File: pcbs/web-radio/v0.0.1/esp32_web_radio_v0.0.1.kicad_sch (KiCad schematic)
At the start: 56 parts, among them IC1 TLV320DAC3100IRHBR, J1 AudioJack4, J3 USB4085-GF-A_REVB, J4 Conn_01x02_Pin, SW1 BOOT, SW2 RESET, SW3 VOLUME_UP, SW6 SW_Slide_DPDT, SW7 VOLUME_DOWN, SW8 MUTE, U1 TLV320AIC3100, U2 ESP32-S3-WROOM-1, U3 AP2127K-1.8, U4 LD39200PUR

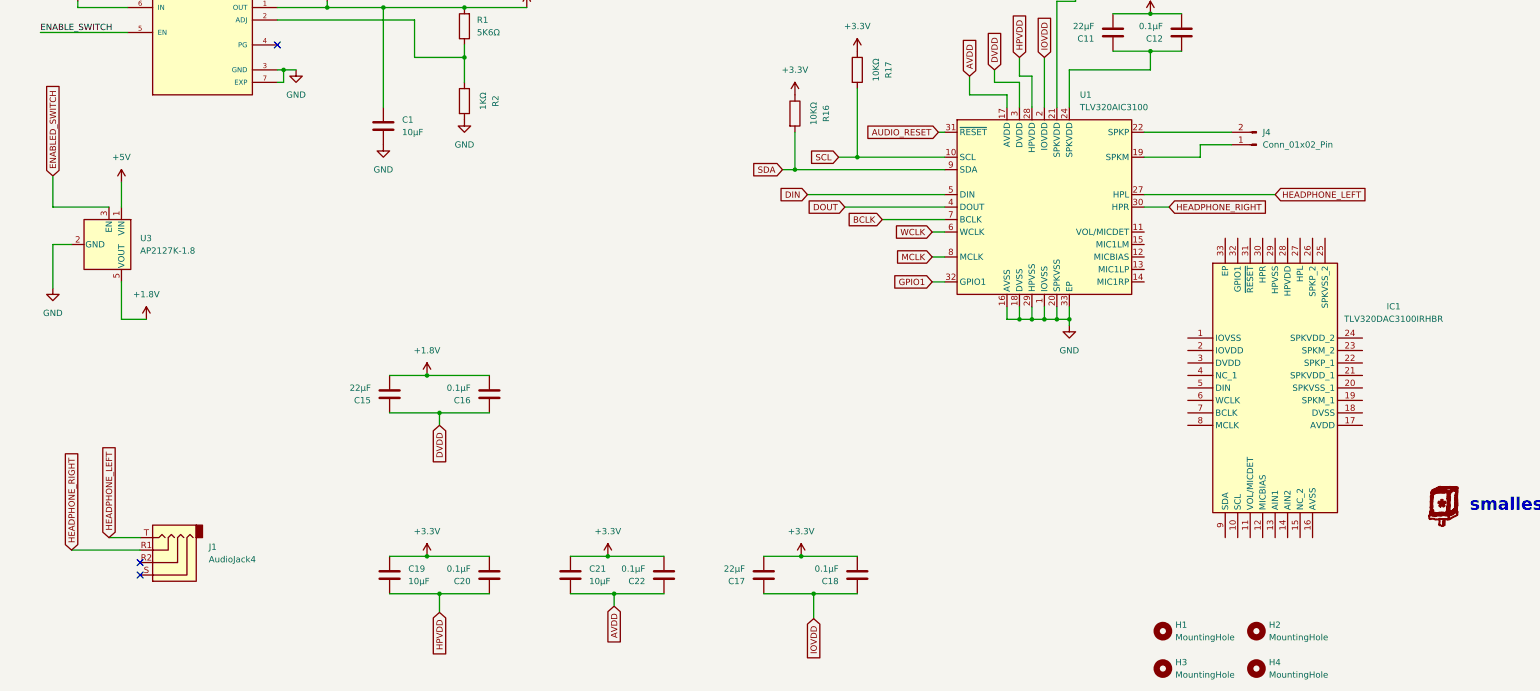
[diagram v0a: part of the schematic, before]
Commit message: adding libraries
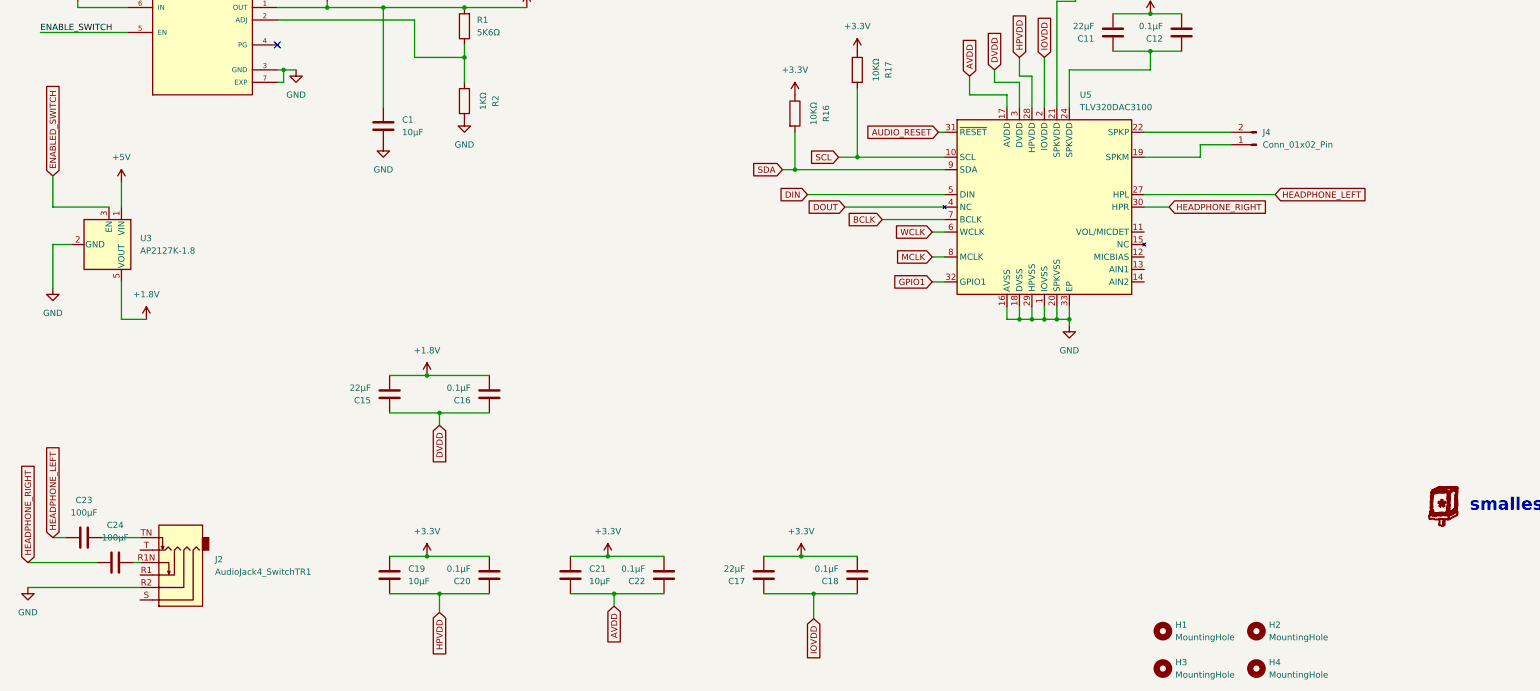
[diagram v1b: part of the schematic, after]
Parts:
- removed IC1: TLV320DAC3100IRHBR, QFN50P500X500X100-33N-D, symbol TLV320DAC:TLV320DAC3100IRHBR
- removed J1: AudioJack4, symbol Connector_Audio:AudioJack4
- removed U1: TLV320AIC3100, Package_DFN_QFN:VQFN-32-1EP_5x5mm_P0.5mm_EP3.5x3.5mm, symbol Audio:TLV320AIC3100
- added C23: 100µF, Capacitor_SMD:C_1206_3216Metric_Pad1.33x1.80mm_HandSolder, symbol Device:C
- added C24: 100µF, Capacitor_SMD:C_0805_2012Metric_Pad1.18x1.45mm_HandSolder, symbol Device:C
- added J2: AudioJack4_SwitchTR1, symbol Connector_Audio:AudioJack4_SwitchTR1
- added U5: TLV320DAC3100, Package_DFN_QFN:VQFN-32-1EP_5x5mm_P0.5mm_EP3.5x3.5mm, symbol smallest-space-hardware/libs:TLV320DAC3100
- J3: footprint USB4085-GF-A_REVB:GCT_USB4085-GF-A_REVB -> smallest-space-hardware/libs:GCT_USB4085-GF-A_REVB
- U4: footprint LD39200PUR:SON95P300X300X100-7N -> smallest-space-hardware/libs:SON95P300X300X100-7N
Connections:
- net AUDIO_RESET: now also U5.31 (~{RESET})
- net AVDD: now also U5.17 (AVDD)
- net BCLK: now also U5.7 (BCLK)
- net DIN: now also U5.5 (DIN)
- net DOUT: now also U5.4 (NC)
- net DVDD: now also U5.3 (DVDD)
- net GND: now also J2.R2, U5.1 (IOVSS), U5.16 (AVSS), U5.18 (DVSS), U5.20 (SPKVSS), U5.25 (SPKVSS), U5.29 (HPVSS), U5.33 (EP)
- net GPIO1: now also U5.32 (GPIO1)
- net HEADPHONE_LEFT: now also C23.2, U5.27 (HPL)
- net HEADPHONE_RIGHT: now also C24.2, U5.30 (HPR)
- net HPVDD: now also U5.28 (HPVDD)
- net IOVDD: now also U5.2 (IOVDD)
- net MCLK: now also U5.8 (MCLK)
- net SCL: now also U5.10 (SCL)
- net SDA: now also U5.9 (SDA)
- net WCLK: now also U5.6 (WCLK)
- net at C13.1, C14.1: now also U5.21 (SPKVDD)
- net at J4.1 (Pin_1): now also U5.19 (SPKM), U5.23 (SPKM)
- net at J4.2 (Pin_2): now also U5.22 (SPKP), U5.26 (SPKP)
- net at C11.1, C12.1: now also U5.24 (SPKVDD)
- new net: C24.1, J2.R1N
- new net: C23.1, J2.TN
- no-connect marks 25 -> 23

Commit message: fix libraries and update schematics
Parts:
- J1: renamed from J3; footprint smallest-space-hardware/libs:GCT_USB4085-GF-A_REVB -> smallest.space:GCT_USB4085-GF-A_REVB
- U2: renamed from U4; footprint smallest-space-hardware/libs:SON95P300X300X100-7N -> smallest.space:SON95P300X300X100-7N
- renumbered C23 to C1, C17 to C10, C6 to C11, C7 to C12, C8 to C13, C18 to C14, C14 to C15, C13 to C16, C11 to C17, C4 to C18, C12 to C19, C24 to C2, C5 to C20, C2 to C21, C3 to C22, C1 to C3, C15 to C4, C19 to C5, C16 to C6, C20 to C7, C21 to C8, C22 to C9, D5 to D1, D4 to D2, D1 to D3, H3 to H2, H2 to H3, J4 to J3, R7 to R1, R6 to R10, R14 to R11, R15 to R12, R3 to R13, R12 to R14, R4 to R15, R8 to R2, R5 to R3, R9 to R4, R1 to R5, R2 to R6, R16 to R7, R13 to R8, R17 to R9, SW6 to SW1, SW3 to SW2, SW7 to SW3, SW8 to SW4, SW2 to SW5, SW1 to SW6, U3 to U1, U5 to U3, U2 to U4
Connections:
- net ENABLE_SWITCH is gone; now on net ENABLED_SWITCH: U2.5 (EN)
- net MICROPHONE_INPUT: now reaches J2.S
- net DOUT: no longer names the net of U4.12 (IO8)
- net DOUT: no longer U3.4 (NC)
- no-connect marks 23 -> 25

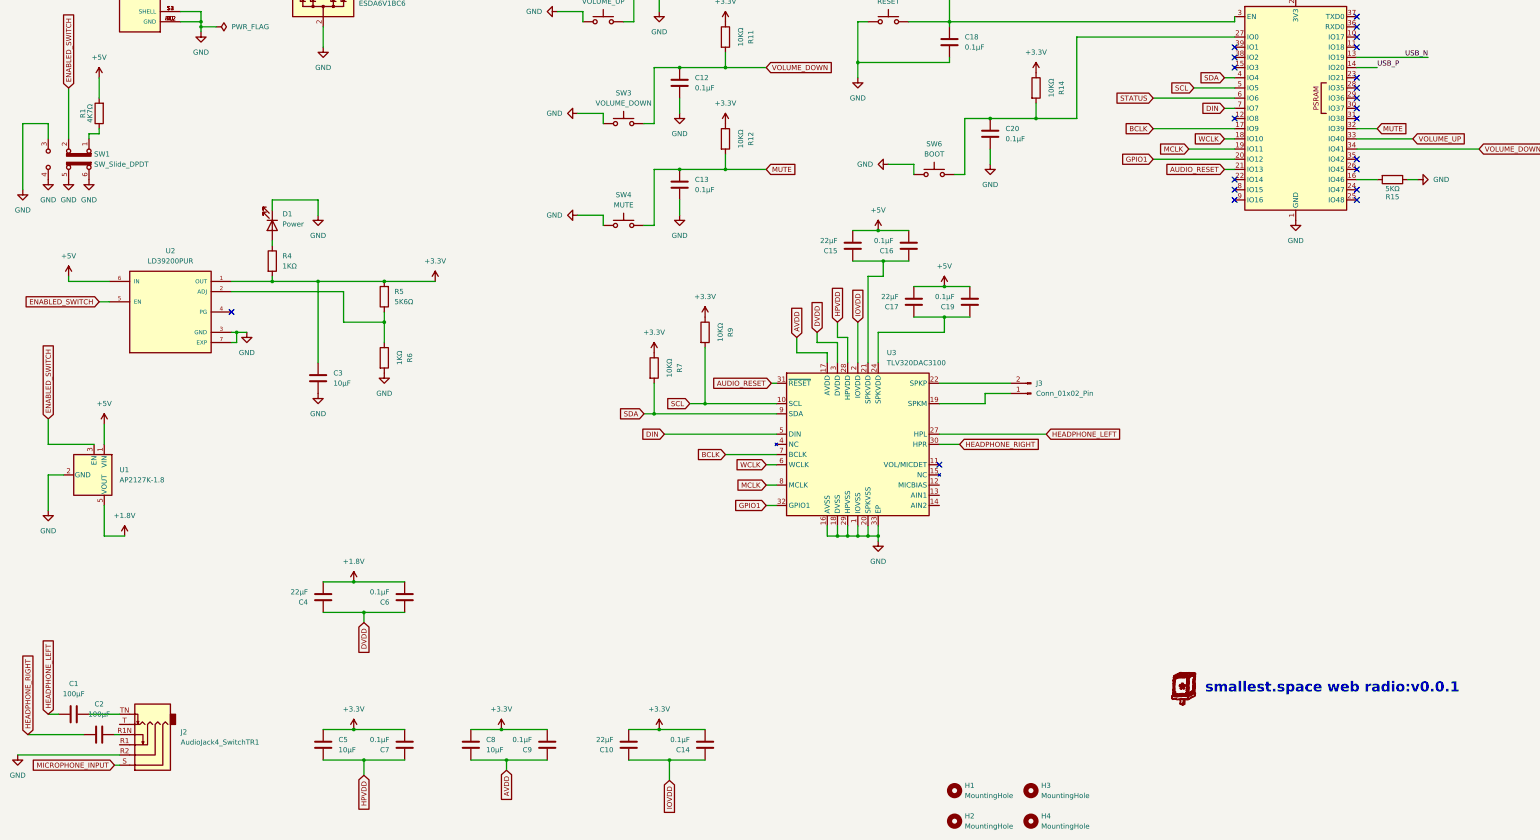
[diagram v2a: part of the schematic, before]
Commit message: switching to some 0603 passives
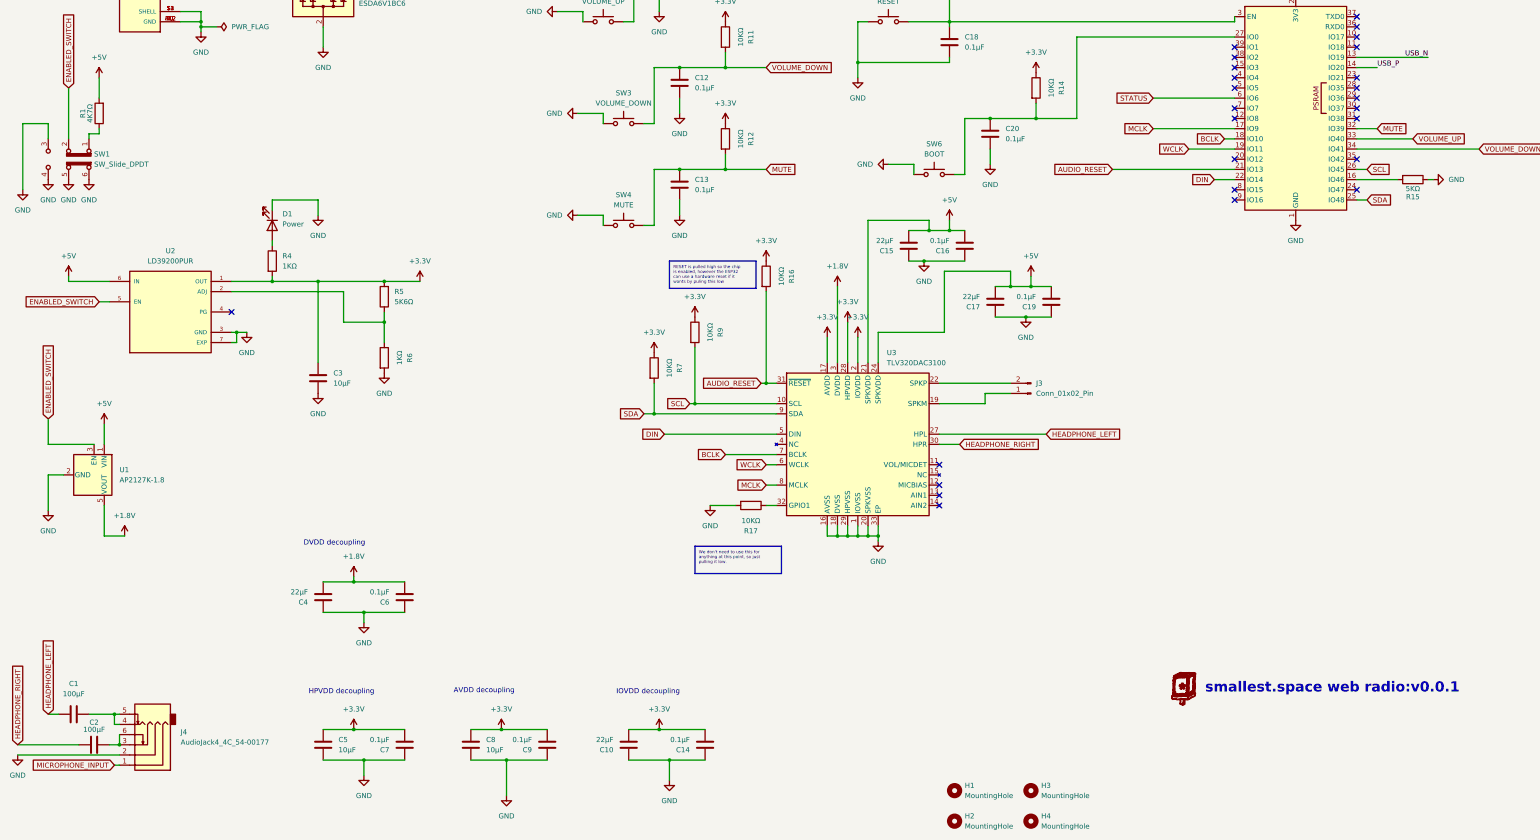
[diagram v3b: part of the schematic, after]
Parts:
- removed J2: AudioJack4_SwitchTR1, symbol Connector_Audio:AudioJack4_SwitchTR1
- added J4: AudioJack4_4C_54-00177, smallest.space:54-00177-headphone-3.5mm-jack, symbol smallest.space:AudioJack4_4C_54-00177
- added R16, R17: 10KΩ, Resistor_SMD:R_0805_2012Metric_Pad1.20x1.40mm_HandSolder, symbol Device:R
- C2: footprint Capacitor_SMD:C_0805_2012Metric_Pad1.18x1.45mm_HandSolder -> Capacitor_SMD:C_1206_3216Metric_Pad1.33x1.80mm_HandSolder
- SW1: footprint (none) -> smallest.space:SLW-913535-2A-SMT
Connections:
- net +1.8V: now also U3.3 (DVDD)
- net +3.3V: now also U3.17 (AVDD), U3.2 (IOVDD), U3.28 (HPVDD), R16.1
- net +5V: now also U3.21 (SPKVDD), U3.24 (SPKVDD)
- net AUDIO_RESET: now also R16.2
- net BCLK: now also U4.18 (IO10); no longer U4.17 (IO9)
- net DIN: now also U4.22 (IO14); no longer U4.7 (IO7)
- net GND: now also C10.1, C14.1, C15.1, C16.1, C17.1, C19.1, C4.1, C5.1, C6.1, C7.1, C8.1, C9.1, J4.2, R17.2
- net MCLK: now also U4.17 (IO9); no longer U4.19 (IO11)
- net MICROPHONE_INPUT: now also J4.1
- net SCL: now also U4.26 (IO45); no longer U4.5 (IO5)
- net SDA: now also U4.25 (IO48); no longer U4.4 (IO4)
- net WCLK: now also U4.19 (IO11); no longer U4.18 (IO10)
- net at C2.1: now also J4.3, J4.6
- net at C1.1: now also J4.4, J4.5
- removed net AVDD: C8.1, C9.1, U3.17 (AVDD)
- removed net DVDD: C4.1, C6.1, U3.3 (DVDD)
- net GPIO1: no longer names the net of U4.20 (IO12)
- net GPIO1: no longer U3.32 (GPIO1)
- removed net HPVDD: C5.1, C7.1, U3.28 (HPVDD)
- removed net IOVDD: C10.1, C14.1, U3.2 (IOVDD)
- new net: R17.1, U3.32 (GPIO1)
- no-connect marks 25 -> 29
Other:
- note added: "AVDD decoupling"
- note added: "DVDD decoupling"
- note added: "HPVDD decoupling"
- note added: "IOVDD decoupling"
- moved on the sheet: C15, C16, C2, R15, R9

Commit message: add version 1
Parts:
- added J2, J5, J6: Conn_01x01_Pin, TestPoint:TestPoint_Pad_1.0x1.0mm, symbol Connector:Conn_01x01_Pin
- C10, C14, C15, C16, C17, C19, C4, C5, C6, C7, C8, C9: footprint Capacitor_SMD:C_0805_2012Metric_Pad1.18x1.45mm_HandSolder -> Capacitor_SMD:C_0603_1608Metric_Pad1.08x0.95mm_HandSolder
- H1, H2, H3, H4: footprint MountingHole:MountingHole_2.5mm -> MountingHole:MountingHole_2.7mm
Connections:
- net +1.8V: now also J6.1 (Pin_1)
- net +3.3V: now also J2.1 (Pin_1)
- net +5V: now also J5.1 (Pin_1)
- net AUDIO_RESET: now also U4.26 (IO45); no longer U4.21 (IO13)
- net BCLK: now also U4.23 (IO21); no longer U4.18 (IO10)
- net DIN: now also U4.25 (IO48); no longer U4.22 (IO14)
- net MCLK: now also U4.22 (IO14); no longer U4.17 (IO9)
- net SCL: now also U4.19 (IO11); no longer U4.26 (IO45)
- net SDA: now also U4.20 (IO12); no longer U4.25 (IO48)
- net VOLUME_DOWN: now also U4.31 (IO38); no longer U4.34 (IO41)
- net WCLK: now also U4.24 (IO47); no longer U4.19 (IO11)
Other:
- moved on the sheet: R15
